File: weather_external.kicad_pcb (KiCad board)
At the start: 2 copper layers, 36 x 76 mm, 19 parts, among them J1 Conn_01x06_Male, J2 Conn_01x02_Male, J3 Conn_01x03_Male, J4 Conn_01x04_Male, Q1 IRF510PBF, SW1 SW_Push, U1 MCP1700-3302E_SOT23, U3 NE555DR

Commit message: Version 1.2. Small components
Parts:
- removed C3, C5: 0.1uF, Capacitor_THT:CP_Radial_D4.0mm_P2.00mm
- removed J1: Conn_01x06_Male, Connector_PinHeader_2.54mm:PinHeader_1x06_P2.54mm_Vertical
- removed Q1: IRF510PBF, digikey-footprints:TO-220-3
- removed the R1 at (29.8, 56.7)
- added C1: 0.1uf, Capacitor_THT:CP_Radial_D4.0mm_P1.50mm, F.Cu at (12.3, 70.5)
- added FTDI1: Conn_01x04_Male, Connector_PinHeader_2.54mm:PinHeader_1x04_P2.54mm_Vertical, F.Cu at (21.0, 84.5)
- added J5: Conn_01x02_Male, Connector_PinHeader_2.54mm:PinHeader_1x02_P2.54mm_Vertical, F.Cu at (21.1, 79.4)
- added L1: INDUCTOR, Inductor_SMD:L_0805_2012Metric_Pad1.15x1.40mm_HandSolder, B.Cu at (12.6, 92.1)
- added R2: 10k, Resistor_SMD:R_1206_3216Metric, B.Cu at (6.35, 91.1)
- added R5: 100k, Resistor_SMD:R_1206_3216Metric, B.Cu at (12.9, 82.8)
- added R6: 270k, Resistor_SMD:R_1206_3216Metric, B.Cu at (12.8, 87.5)
- C2: value 220uF -> 47uf; footprint Capacitor_THT:CP_Radial_D4.0mm_P2.00mm -> Capacitor_THT:CP_Radial_D4.0mm_P1.50mm
- J2: footprint Connector_PinHeader_2.54mm:PinHeader_1x02_P2.54mm_Vertical -> Connector_JST:JST_PH_B2B-PH-K_1x02_P2.00mm_Vertical
- R3, R4: footprint Resistor_THT:R_Axial_DIN0207_L6.3mm_D2.5mm_P7.62mm_Horizontal -> Resistor_SMD:R_1206_3216Metric; moved to B.Cu
- U1: moved to B.Cu
- U3: footprint Package_DIP:DIP-8_W7.62mm -> Package_SO:SOIC-8_3.9x4.9mm_P1.27mm; moved to B.Cu
- moved C2 41.7 mm to (2.25, 71.5)
- moved R3 36.7 mm to (6.15, 87.8), turned to 0 degrees
- moved C4 30.9 mm to (7.25, 71.7)
- moved J3 30.5 mm to (20.4, 66.3), turned to 0 degrees
- moved J2 25.9 mm to (3.92, 52.9), turned to 180 degrees
- moved SW1 25.1 mm to (15.1, 66.3)
- moved R4 23.7 mm to (12.9, 79.0), turned to 180 degrees
- moved U1 23.4 mm to (13.3, 53.2)
- moved U3 23.2 mm to (6.47, 81.6), turned to 270 degrees
- moved I2C1 11.2 mm to (9.05, 57.4)
- moved RV1 10.0 mm to (3.12, 56.6)
- moved ESP8266-12E1 4.29 mm to (9.32, 86.9), turned to 180 degrees
- moved JP1 4.13 mm to (1.20, 65.2), turned to 90 degrees
- moved R1 2.37 mm to (9.38, 53.4), turned to 0 degrees
- renumbered J4 to I2C1, R5 to R1
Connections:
- C2 pad 1: Net-(C2-Pad1) -> +3V3
- ESP8266-12E1 pad 1: Net-(C2-Pad1) -> Net-(ESP8266-12E1-Pad1)
- ESP8266-12E1 pad 2: (no net) -> Net-(ESP8266-12E1-Pad2)
- ESP8266-12E1 pad 8: Net-(C3-Pad1) -> Net-(C1-Pad1)
- I2C1 pad 1: Net-(C3-Pad1) -> +3V3
- J3 pad 1: Net-(C3-Pad1) -> +3V3
- R3 pad 1: Net-(ESP8266-12E1-Pad3) -> +3V3
- R3 pad 2: Net-(C3-Pad1) -> Net-(ESP8266-12E1-Pad3)
- R4 pad 1: Net-(C2-Pad1) -> +3V3
- R4 pad 2: Net-(C3-Pad1) -> Net-(ESP8266-12E1-Pad17)
- RV1 pad 2: VCC -> Net-(JP1-Pad1)
- SW1 pad 1: Net-(C2-Pad1) -> Net-(ESP8266-12E1-Pad1)
- U1 pad 2: Net-(C3-Pad1) -> +3V3
- U3 pad 3: Net-(C2-Pad1) -> Net-(ESP8266-12E1-Pad1)
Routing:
- net Net-(C3-Pad1): track 124.6 -> 0.00 mm, vias 1 -> 0
- net Net-(ESP8266-12E1-Pad1): track 0.00 -> 106.9 mm, vias 0 -> 3
- net +3V3: track 0.00 -> 99.2 mm, vias 0 -> 2
- net Net-(C2-Pad1): track 94.3 -> 0.00 mm
- net Net-(JP1-Pad1): track 18.1 -> 53.1 mm
- net Net-(C1-Pad1): track 0.00 -> 33.9 mm, vias 0 -> 1
- net Net-(ESP8266-12E1-Pad3): track 38.5 -> 9.66 mm
- net Net-(ESP8266-12E1-Pad18): track 5.17 -> 31.6 mm, vias 0 -> 1
- net Net-(ESP8266-12E1-Pad17): track 39.0 -> 13.7 mm
- net Net-(R1-Pad1): track 14.9 -> 38.0 mm, vias 0 -> 4
- net Net-(J3-Pad3): track 4.50 -> 24.0 mm
- net VCC: track 53.6 -> 69.6 mm
- net Net-(J1-Pad6): track 15.4 -> 0.00 mm
- net Net-(ESP8266-12E1-Pad2): track 0.00 -> 15.0 mm, vias 0 -> 1
- net Net-(ESP8266-12E1-Pad20): track 30.1 -> 42.4 mm
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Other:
- board size 36 x 76 mm -> 26 x 48 mm
- board text added: "IO0"
- board text added: "RST"
- board text added: "Weather External V1.2"
- board text removed: "555 on/off"
- board text removed: "DTR"
- board text removed: "FTDI"
- board text removed: "GND"
- board text removed: "RTS"
- board text removed: "VCC"
- board text removed: "Weather External V1.0"

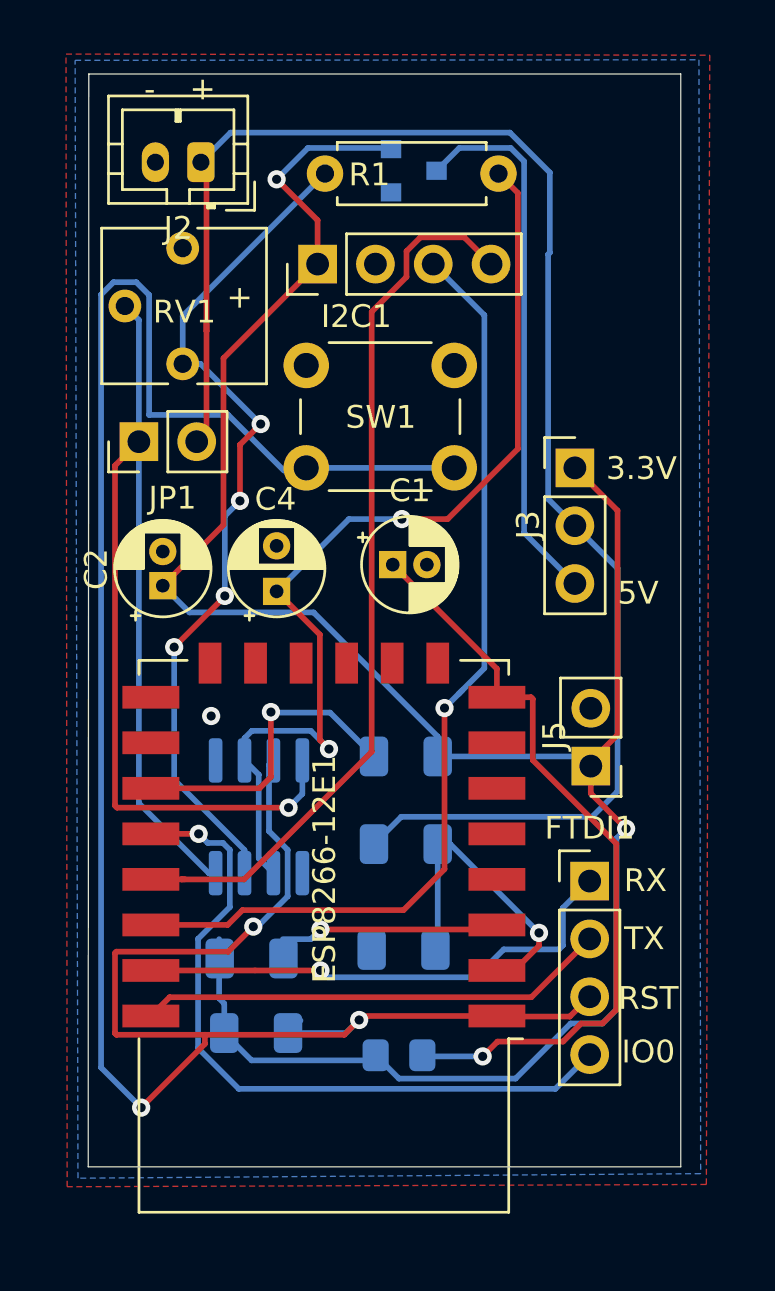
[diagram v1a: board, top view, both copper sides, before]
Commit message: Version with 555
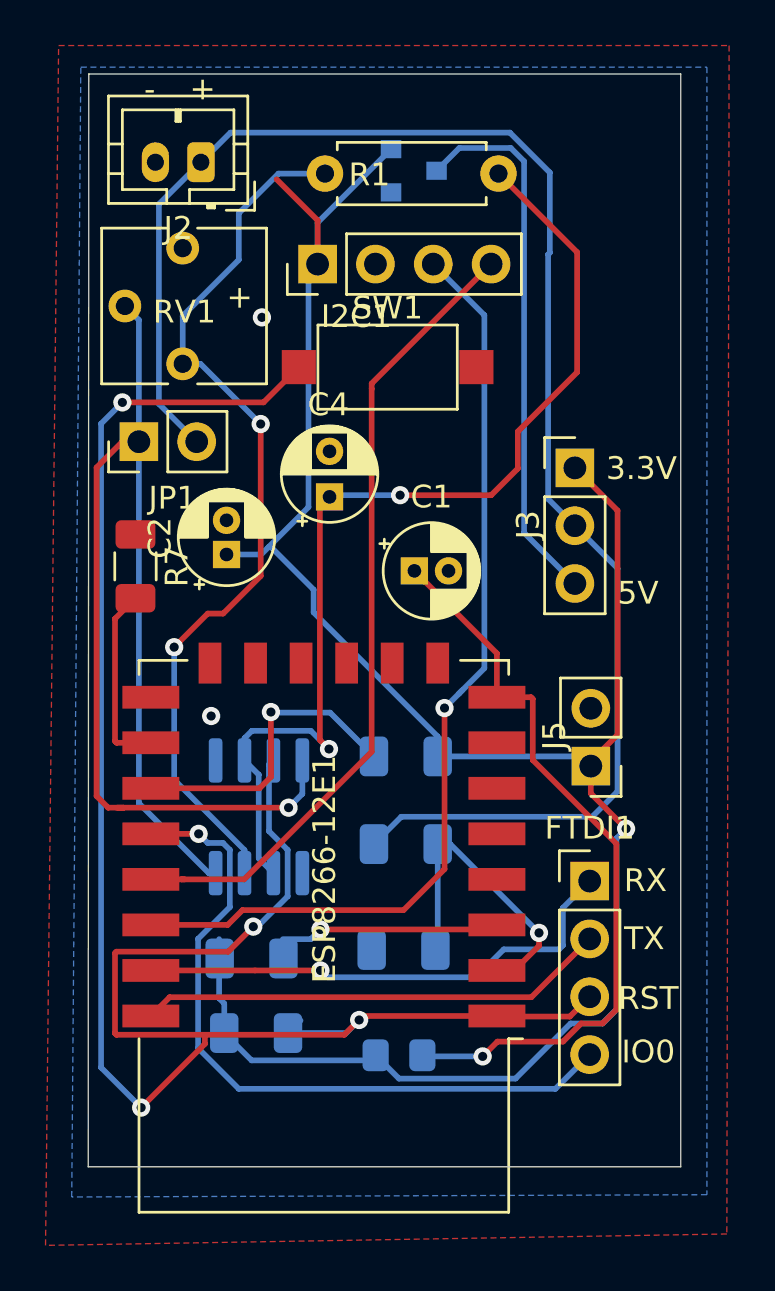
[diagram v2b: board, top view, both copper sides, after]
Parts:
- added R7: 5k, Resistor_SMD:R_1206_3216Metric, F.Cu at (1.05, 70.6)
- R2, R3, R4: value 10k -> 5k
- SW1: footprint Button_Switch_THT:SW_PUSH_6mm -> Button_Switch_SMD:SW_SPST_CK_RS282G05A3
- moved SW1 5.30 mm to (12.1, 61.9), turned to 0 degrees
- moved C4 4.76 mm to (9.57, 67.6)
- moved C2 3.12 mm to (5.05, 70.1)
- moved C1 0.99 mm to (13.3, 70.8)
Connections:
- ESP8266-12E1 pad 16: GND -> Net-(ESP8266-12E1-Pad16)
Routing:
- net Net-(ESP8266-12E1-Pad1): track 106.9 -> 89.8 mm, vias 3 -> 4
- net Net-(ESP8266-12E1-Pad16): track 0.00 -> 8.25 mm
- net +3V3: track 99.2 -> 95.1 mm, vias 2 -> 1
- net Net-(ESP8266-12E1-Pad19): track 39.2 -> 35.8 mm
- net Net-(C4-Pad1): track 44.6 -> 46.4 mm
- net VCC: track 69.6 -> 71.4 mm
- net Net-(JP1-Pad1): track 53.1 -> 54.8 mm
- net Net-(R1-Pad1): track 38.0 -> 39.6 mm, vias 4 -> 2
- net Net-(C1-Pad1): track 33.9 -> 33.2 mm
- net GND: vias 1 -> 2

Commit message: SMD Components
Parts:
- removed C4: 220uf, Capacitor_THT:CP_Radial_D4.0mm_P2.00mm
- removed J3: Conn_01x03_Male, Connector_PinHeader_2.54mm:PinHeader_1x03_P2.54mm_Vertical
- removed J5: Conn_01x02_Male, Connector_PinHeader_2.54mm:PinHeader_1x02_P2.54mm_Vertical
- removed R1: 220, Resistor_THT:R_Axial_DIN0207_L6.3mm_D2.5mm_P7.62mm_Horizontal
- removed RV1: 1M, Potentiometer_THT:Potentiometer_Vishay_T73YP_Vertical
- removed U1: MCP1700-3302E_SOT23, Package_TO_SOT_SMD:SOT-23
- removed U3: NE555DR, Package_SO:SOIC-8_3.9x4.9mm_P1.27mm
- JP1: value Jumper_2_Open -> Jumper_NO_Small
- L1, R2, R3, R4, R5, R6: moved to F.Cu
- moved JP1 36.3 mm to (-1.02, 101.3), turned to 180 degrees
- moved I2C1 31.1 mm to (-0.76, 86.9), turned to 180 degrees
- moved R2 30.3 mm to (11.2, 61.2), turned to 180 degrees
- moved FTDI1 28.0 mm to (-6.10, 91.7), turned to 180 degrees
- moved R6 23.7 mm to (26.4, 68.1)
- moved R5 22.9 mm to (26.3, 64.3)
- moved R3 21.0 mm to (18.5, 70.9)
- moved L1 18.2 mm to (12.4, 73.9)
- moved SW1 17.3 mm to (-5.08, 63.2), turned to 90 degrees
- moved R4 11.8 mm to (2.29, 73.9)
- moved J2 6.96 mm to (10.7, 54.6)
- moved R7 6.56 mm to (7.37, 72.4)
- moved ESP8266-12E1 5.63 mm to (14.5, 89.2)
- moved C2 4.20 mm to (6.10, 66.0), turned to 270 degrees
- moved C1 3.53 mm to (13.0, 67.3)
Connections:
- ESP8266-12E1 pad 4: (no net) -> Net-(ESP8266-12E1-Pad4)
- J2 pad 1: VCC -> +3V3
- JP1 pad 1: Net-(JP1-Pad1) -> Net-(ESP8266-12E1-Pad1)
- JP1 pad 2: VCC -> Net-(ESP8266-12E1-Pad4)
- R5 pad 1: VCC -> +3V3
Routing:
- net VCC: track 71.4 -> 0.00 mm
- net Net-(JP1-Pad1): track 54.8 -> 0.00 mm, vias 1 -> 0
- net Net-(C4-Pad1): track 46.4 -> 0.00 mm, vias 2 -> 0
- net Net-(R1-Pad1): track 39.6 -> 0.00 mm, vias 2 -> 0
- net Net-(ESP8266-12E1-Pad20): track 42.4 -> 12.0 mm, vias 1 -> 0
- net Net-(ESP8266-12E1-Pad4): track 0.00 -> 29.9 mm
- net Net-(J3-Pad3): track 24.0 -> 0.00 mm
- net Net-(ESP8266-12E1-Pad19): track 35.8 -> 12.2 mm
- net GND: track 0.00 -> 19.2 mm, vias 2 -> 4
- net Net-(ESP8266-12E1-Pad2): track 15.0 -> 30.3 mm, vias 1 -> 0
- net Net-(C1-Pad1): track 33.2 -> 19.4 mm, vias 1 -> 0
- net Net-(ESP8266-12E1-Pad18): track 31.6 -> 44.9 mm, vias 1 -> 0
- net Net-(ESP8266-12E1-Pad3): track 9.66 -> 22.6 mm, vias 1 -> 0
- net Net-(ESP8266-12E1-Pad21): track 22.1 -> 13.4 mm, vias 1 -> 0
- net Net-(ESP8266-12E1-Pad1): track 89.8 -> 97.9 mm, vias 4 -> 0
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- removed copper zone on B.Cu, net GND
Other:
- board outline removed
- board text removed: "-"
- board text removed: "3.3V"
- board text removed: "5V"
- board text removed: "IO0"
- board text removed: "RST"
- board text removed: "RX"
- board text removed: "TX"

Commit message: no 555 Print version
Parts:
- removed L1: INDUCTOR, Inductor_SMD:L_0805_2012Metric_Pad1.15x1.40mm_HandSolder
- added J1: Conn_01x02_Male, Connector_PinHeader_2.54mm:PinHeader_1x02_P2.54mm_Vertical, F.Cu at (10.9, 60.7)
- added R1: 5k, Resistor_THT:R_Axial_DIN0207_L6.3mm_D2.5mm_P7.62mm_Horizontal, F.Cu at (-7.11, 72.6)
- R2, R3, R4, R5, R6, R7: footprint Resistor_SMD:R_1206_3216Metric -> Resistor_THT:R_Axial_DIN0207_L6.3mm_D2.5mm_P7.62mm_Horizontal
- SW1: footprint Button_Switch_SMD:SW_SPST_CK_RS282G05A3 -> Button_Switch_THT:SW_PUSH_6mm
- moved R4 12.2 mm to (-1.27, 62.2), turned to 270 degrees
- moved C1 9.20 mm to (17.3, 59.2)
- moved R2 8.99 mm to (5.08, 54.6)
- moved R6 8.19 mm to (22.4, 61.0), turned to 270 degrees
- moved R3 7.64 mm to (11.4, 68.1)
- moved C2 6.59 mm to (3.05, 60.2)
- moved R7 6.12 mm to (6.86, 66.3)
- moved I2C1 4.33 mm to (-3.56, 83.6)
- moved SW1 4.10 mm to (-8.89, 64.8)
- moved FTDI1 3.45 mm to (-7.11, 95.0)
- moved R5 3.32 mm to (25.9, 61.0), turned to 270 degrees
- moved J2 1.52 mm to (10.7, 56.1)
- moved JP1 1.02 mm to (-1.02, 100.3)
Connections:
- C1 pad 1: Net-(C1-Pad1) -> +3V3
- ESP8266-12E1 pad 8: Net-(C1-Pad1) -> +3V3
- FTDI1 pad 1: Net-(ESP8266-12E1-Pad21) -> Net-(ESP8266-12E1-Pad18)
- FTDI1 pad 3: Net-(ESP8266-12E1-Pad1) -> Net-(ESP8266-12E1-Pad21)
- FTDI1 pad 4: Net-(ESP8266-12E1-Pad18) -> Net-(ESP8266-12E1-Pad1)
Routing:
- net +3V3: track 96.0 -> 116.1 mm
- net Net-(C1-Pad1): track 19.4 -> 0.00 mm
- net Net-(ESP8266-12E1-Pad1): track 97.9 -> 86.4 mm
- net Net-(ESP8266-12E1-Pad22): track 23.5 -> 15.1 mm
- net GND: track 19.2 -> 11.3 mm, vias 4 -> 2
- net Net-(ESP8266-12E1-Pad19): track 12.2 -> 19.2 mm
- net Net-(ESP8266-12E1-Pad17): track 12.5 -> 19.3 mm
- net Net-(ESP8266-12E1-Pad20): track 12.0 -> 17.8 mm
- net Net-(ESP8266-12E1-Pad3): track 22.6 -> 25.8 mm
- net Net-(ESP8266-12E1-Pad4): track 29.9 -> 27.7 mm
- net Net-(ESP8266-12E1-Pad21): track 13.4 -> 14.3 mm
- net Net-(ESP8266-12E1-Pad2): track 30.3 -> 29.5 mm
- net Net-(ESP8266-12E1-Pad18): track 44.9 -> 44.3 mm
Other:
- board outline added: 40.6 x 51.9 mm

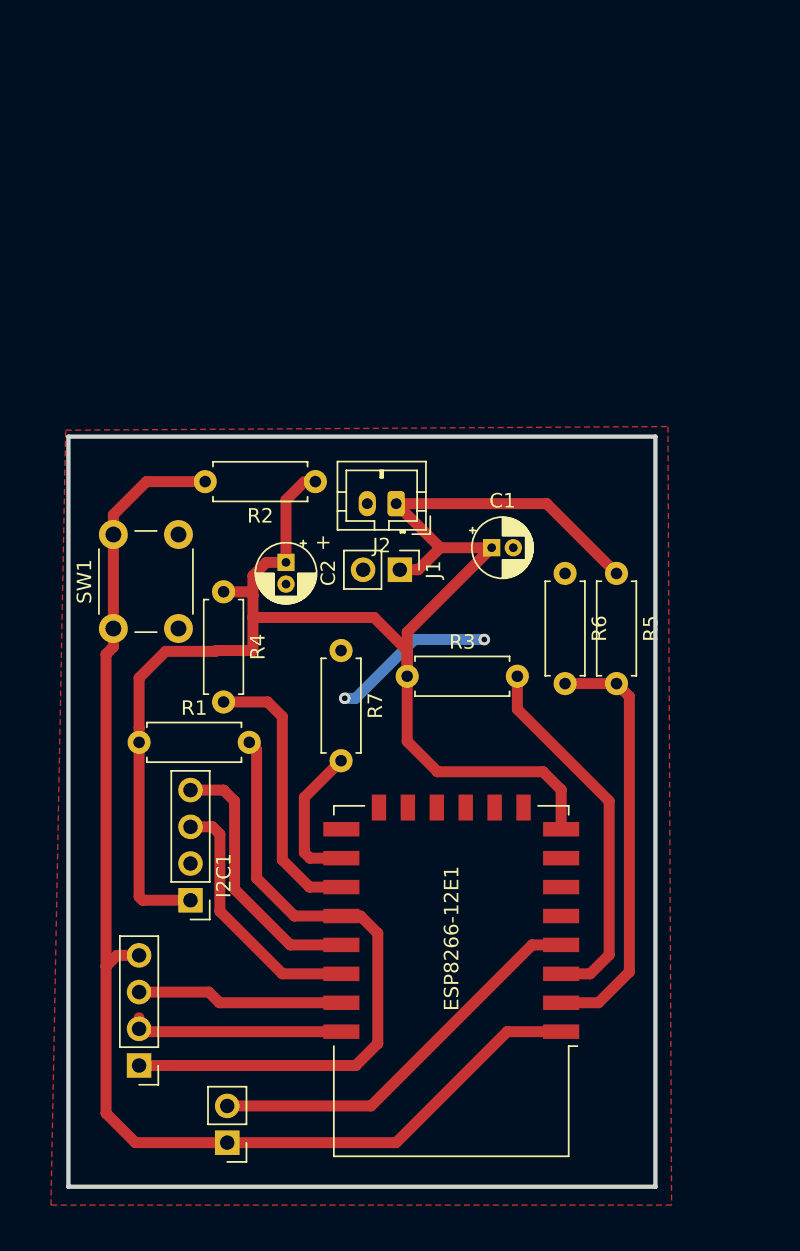
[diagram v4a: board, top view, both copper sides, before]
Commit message: No 555 print version
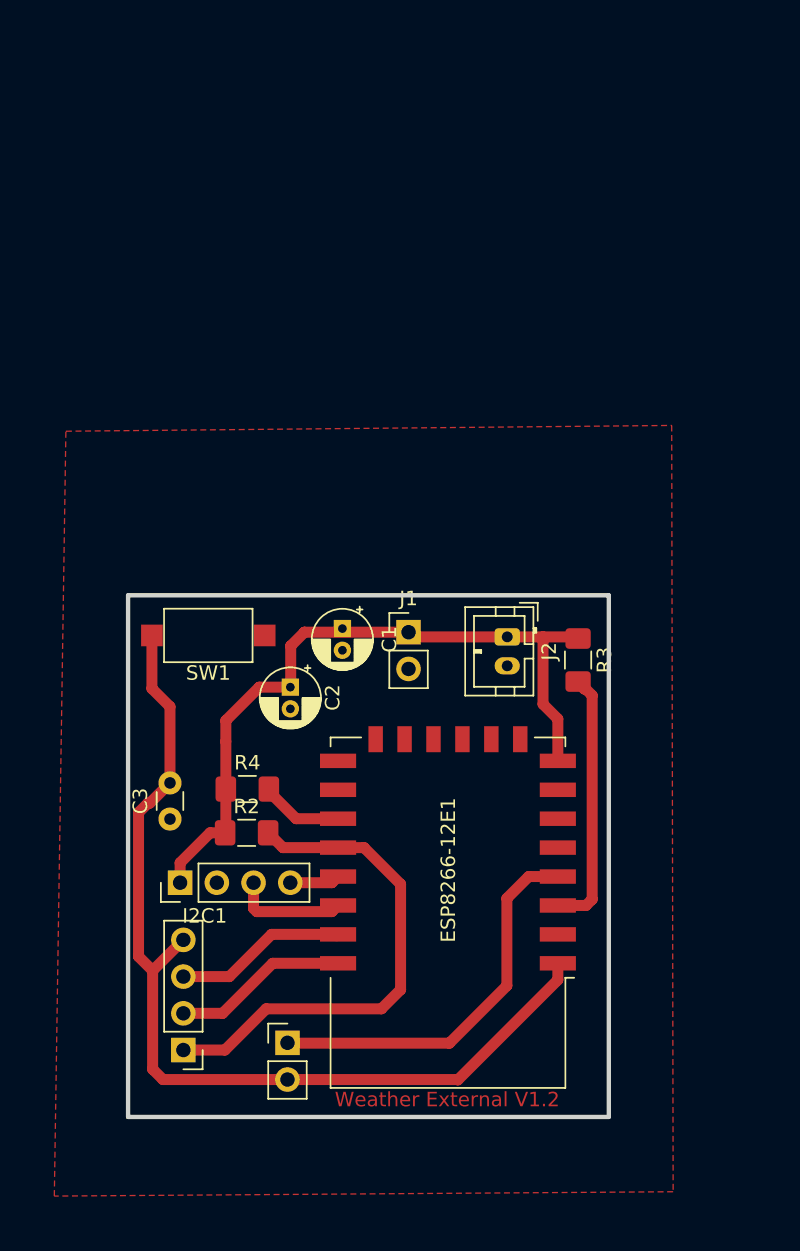
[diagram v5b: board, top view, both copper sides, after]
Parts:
- removed R1, R7: 5k, Resistor_THT:R_Axial_DIN0207_L6.3mm_D2.5mm_P7.62mm_Horizontal
- removed R5: 100k, Resistor_THT:R_Axial_DIN0207_L6.3mm_D2.5mm_P7.62mm_Horizontal
- removed R6: 270k, Resistor_THT:R_Axial_DIN0207_L6.3mm_D2.5mm_P7.62mm_Horizontal
- added C3: 100nf, Capacitor_THT:C_Disc_D3.0mm_W1.6mm_P2.50mm, F.Cu at (-4.97, 78.0)
- R2, R3, R4: value 5k -> 12k; footprint Resistor_THT:R_Axial_DIN0207_L6.3mm_D2.5mm_P7.62mm_Horizontal -> Resistor_SMD:R_1206_3216Metric_Pad1.42x1.75mm_HandSolder
- SW1: footprint Button_Switch_THT:SW_PUSH_6mm -> Button_Switch_SMD:SW_SPST_CK_RS282G05A3
- moved R2 24.8 mm to (0.33, 78.9), turned to 0 degrees
- moved R4 13.7 mm to (0.38, 75.9), turned to 0 degrees
- moved J2 12.0 mm to (18.4, 65.3), turned to 270 degrees
- moved R3 11.9 mm to (23.2, 67.0), turned to 270 degrees
- moved C1 11.7 mm to (6.95, 64.8), turned to 270 degrees
- moved C2 8.63 mm to (3.35, 68.8)
- moved JP1 8.06 mm to (3.15, 93.4), turned to 0 degrees
- moved SW1 6.58 mm to (-2.33, 65.2), turned to 180 degrees
- moved ESP8266-12E1 4.73 mm to (14.2, 84.4)
- moved J1 4.36 mm to (11.5, 65.0), turned to 0 degrees
- moved FTDI1 3.24 mm to (-4.05, 93.9)
- moved I2C1 1.41 mm to (-4.28, 82.3), turned to 90 degrees
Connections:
- net Net-(ESP8266-12E1-Pad17) renamed GPIO2
- net Net-(ESP8266-12E1-Pad19) renamed SDA
- net Net-(ESP8266-12E1-Pad20) renamed SCL
- net Net-(ESP8266-12E1-Pad21) renamed RX
- net Net-(ESP8266-12E1-Pad22) renamed TX
- net Net-(ESP8266-12E1-Pad3) renamed EN
- C1 pad 2: GND -> GPIO15
- C2 pad 2: GND -> GPIO15
- ESP8266-12E1 pad 1: Net-(ESP8266-12E1-Pad1) -> RST
- ESP8266-12E1 pad 15: GND -> GPIO15
- ESP8266-12E1 pad 16: Net-(ESP8266-12E1-Pad16) -> GPIO15
- ESP8266-12E1 pad 18: Net-(ESP8266-12E1-Pad18) -> GPIO0
- ESP8266-12E1 pad 2: Net-(ESP8266-12E1-Pad2) -> (no net)
- ESP8266-12E1 pad 4: Net-(ESP8266-12E1-Pad4) -> GPIO16
- FTDI1 pad 1: Net-(ESP8266-12E1-Pad18) -> GPIO0
- FTDI1 pad 4: Net-(ESP8266-12E1-Pad1) -> RST
- I2C1 pad 2: GND -> GPIO15
- J1 pad 2: GND -> GPIO15
- J2 pad 2: GND -> GPIO15
- JP1 pad 1: Net-(ESP8266-12E1-Pad1) -> GPIO16
- JP1 pad 2: Net-(ESP8266-12E1-Pad4) -> RST
- R2 pad 2: Net-(ESP8266-12E1-Pad1) -> GPIO0
- SW1 pad 1: Net-(ESP8266-12E1-Pad1) -> GPIO15
- SW1 pad 2: GND -> RST
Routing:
- net Net-(ESP8266-12E1-Pad1): track 86.4 -> 0.00 mm
- net RST: track 0.00 -> 67.2 mm
- net +3V3: track 116.1 -> 51.0 mm
- net Net-(ESP8266-12E1-Pad18): track 44.3 -> 0.00 mm
- net GPIO0: track 0.00 -> 34.7 mm
- net Net-(ESP8266-12E1-Pad2): track 29.5 -> 0.00 mm
- net Net-(ESP8266-12E1-Pad4): track 27.7 -> 0.00 mm
- net GPIO16: track 0.00 -> 27.0 mm
- net SDA: track 19.2 -> 3.48 mm
- net GPIO2: track 19.3 -> 5.73 mm
- net GND: track 11.3 -> 0.00 mm, vias 2 -> 0
- net Net-(ESP8266-12E1-Pad16): track 10.9 -> 0.00 mm
- net SCL: track 17.8 -> 7.89 mm
- net EN: track 25.8 -> 18.1 mm
- net TX: track 15.1 -> 12.1 mm
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- added copper zone on F.Cu, net GPIO15
- removed copper zone on F.Cu, net GND
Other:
- board size 40.6 x 51.9 mm -> 33.2 x 36.1 mm
- board text removed: "+"

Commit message: JLCPCB version 1.3
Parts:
- JP1: footprint Connector_PinHeader_2.54mm:PinHeader_1x02_P2.54mm_Vertical -> Jumper:SolderJumper-2_P1.3mm_Open_Pad1.0x1.5mm; moved to B.Cu
- R2, R3, R4, SW1: moved to B.Cu
- moved J1 20.7 mm to (1.10, 82.9), turned to 270 degrees
- moved JP1 18.5 mm to (21.6, 94.8), turned to 180 degrees
- moved R3 15.5 mm to (17.2, 81.2)
- moved R4 13.8 mm to (14.2, 75.8), turned to 180 degrees
- moved R2 12.0 mm to (12.1, 81.1), turned to 90 degrees
- moved C3 8.67 mm to (3.65, 78.9), turned to 180 degrees
- moved I2C1 8.58 mm to (3.15, 86.7), turned to 0 degrees
- moved SW1 7.05 mm to (2.35, 70.5), turned to 90 degrees
- moved C1 6.06 mm to (12.1, 68.0)
- moved C2 3.74 mm to (7.00, 68.0)
- moved FTDI1 2.65 mm to (-1.43, 94.2)
- moved J2 2.28 mm to (17.5, 67.5), turned to 0 degrees
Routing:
- net SDA: track 3.48 -> 17.1 mm
- net RST: track 67.2 -> 54.6 mm, vias 0 -> 1
- net EN: track 18.1 -> 6.03 mm, vias 0 -> 1
- net +3V3: track 51.0 -> 58.6 mm, vias 0 -> 1
- net GPIO16: track 27.0 -> 21.4 mm, vias 0 -> 1
- net SCL: track 7.89 -> 12.6 mm
- net GPIO0: track 34.7 -> 30.9 mm, vias 0 -> 1
- net RX: track 12.1 -> 9.42 mm
- net TX: track 12.1 -> 9.64 mm
- net GPIO2: track 5.73 -> 6.92 mm, vias 0 -> 1
- added copper zone on B.Cu, net GPIO15
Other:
- board size 33.2 x 36.1 mm -> 28.2 x 33.8 mm
- board text added: "+"
- board text added: "-"
- board text added: "EN/DIS deepsleep"
- board text added: "IO0"
- board text added: "RST"
- board text added: "RX"
- board text added: "SCL"
- board text added: "SDA"
- board text added: "TX"
- board text added: "Weather External v1.3"
- board text removed: "Weather External V1.2"
